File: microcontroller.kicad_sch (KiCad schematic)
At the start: 13 parts, among them SW3 System Reset, SW4 Boot Switch, U1 STM32F446RETx

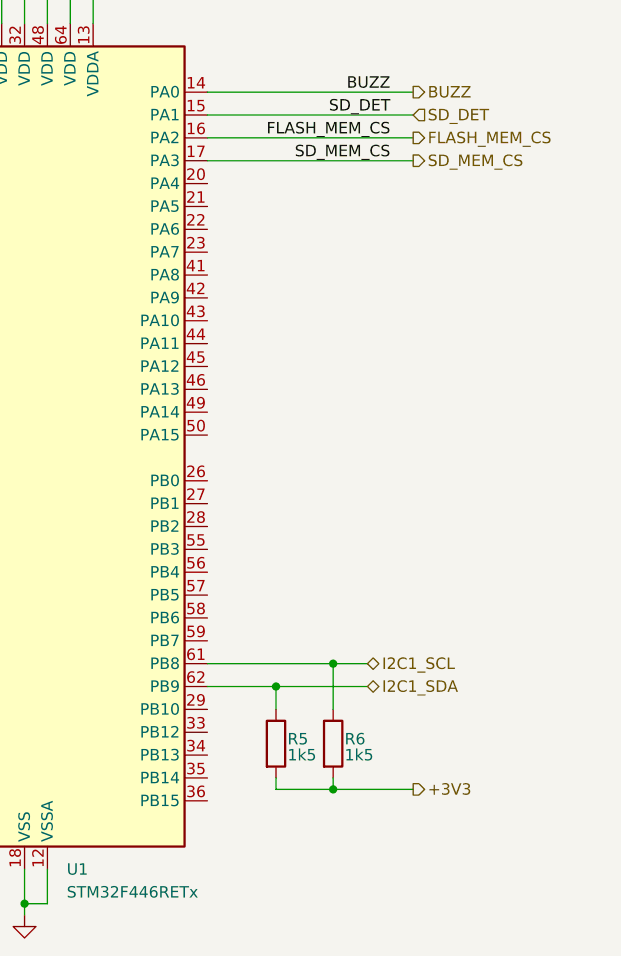
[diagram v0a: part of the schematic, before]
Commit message: more boilerplate for stm. and also power supply using LDO and USB
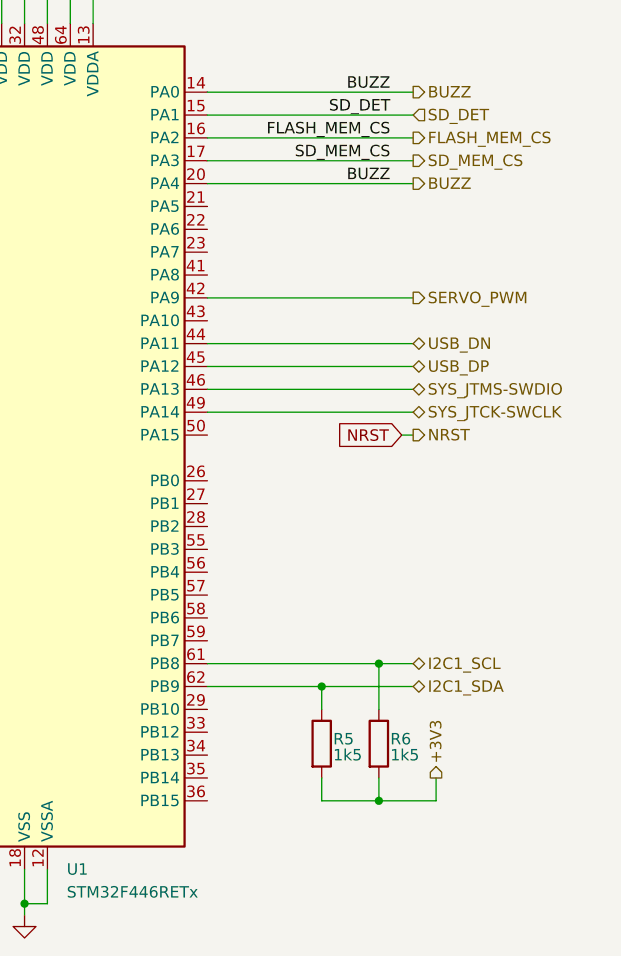
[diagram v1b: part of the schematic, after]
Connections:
- net BUZZ: now also U1.20 (PA4)
- net SERVO_PWM: now reaches U1.42 (PA9)
- net USB_DN: now reaches U1.44 (PA11)
- net USB_DP: now reaches U1.45 (PA12)
- net SYS_JTMS-SWDIO: now reaches U1.46 (PA13)
- net SYS_JTCK-SWCLK: now reaches U1.49 (PA14)
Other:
- moved on the sheet: R5, R6

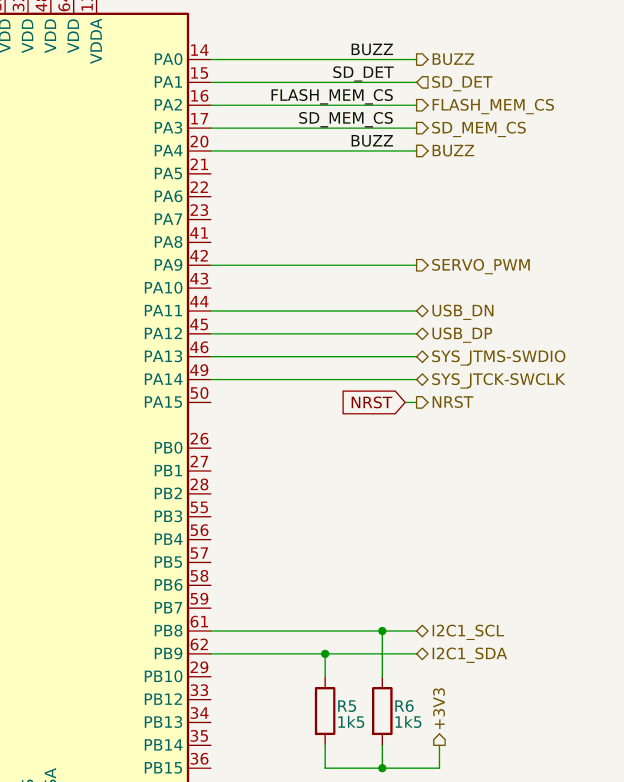
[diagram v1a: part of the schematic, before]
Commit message: base mcu decoupling cap routing
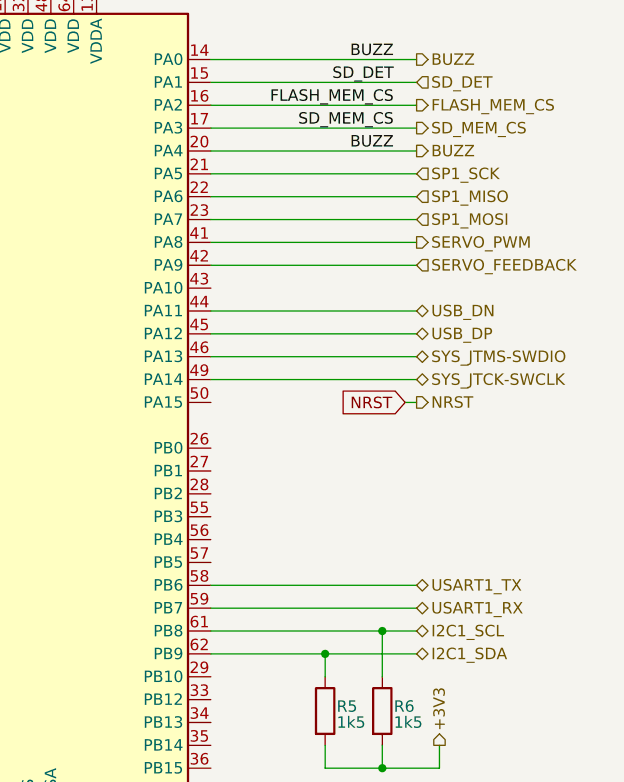
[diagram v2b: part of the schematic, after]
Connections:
- net SERVO_PWM: now also U1.41 (PA8); no longer U1.42 (PA9)
- net SP1_SCK: now reaches U1.21 (PA5)
- net SP1_MISO: now reaches U1.22 (PA6)
- net SP1_MOSI: now reaches U1.23 (PA7)
- net USART1_TX: now reaches U1.58 (PB6)
- net USART1_RX: now reaches U1.59 (PB7)
- new net SERVO_FEEDBACK: U1.42 (PA9)
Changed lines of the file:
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@@
+	(wire
+		(pts
+			(xy 146.05 133.35) (xy 168.91 133.35)
+		)
+		(stroke
+			(width 0)
+			(type default)
+		)
+	)
 	(wire
 		(pts
@@
 	(wire
 		(pts
+			(xy 146.05 130.81) (xy 168.91 130.81)
+		)
+		(stroke
+			(width 0)
+			(type default)
+		)
+	)
+	(wire
+		(pts
 			(xy 54.61 38.1) (xy 54.61 35.56)
 		)
@@
 	(wire
 		(pts
+			(xy 146.05 95.25) (xy 168.91 95.25)
+		)
+		(stroke
+			(width 0)
+			(type default)
+		)
+	)
+	(wire
+		(pts
 			(xy 158.75 138.43) (xy 168.91 138.43)
 		)
@@
 	(wire
 		(pts
+			(xy 146.05 85.09) (xy 168.91 85.09)
+		)
+		(stroke
+			(width 0)
+			(type default)
+		)
+	)
+	(wire
+		(pts
 			(xy 68.58 72.39) (xy 76.2 72.39)
 		)
@@
 	(wire
 		(pts
+			(xy 146.05 87.63) (xy 168.91 87.63)
+		)
+		(stroke
+			(width 0)
+			(type default)
+		)
+	)
+	(wire
+		(pts
 			(xy 130.81 60.96) (xy 133.35 60.96)
 		)
@@
 	(wire
 		(pts
-			(xy 146.05 95.25) (xy 168.91 95.25)
-		)
-		(stroke
-			(width 0)
-			(type default)
-		)
-	)
-	(wire
-		(pts
 			(xy 57.15 74.93) (xy 58.42 74.93)
 		)
@@
 	(wire
 		(pts
+			(xy 146.05 92.71) (xy 168.91 92.71)
+		)
+		(stroke
+			(width 0)
+			(type default)
+		)
+	)
+	(wire
+		(pts
 			(xy 146.05 138.43) (xy 158.75 138.43)
 		)
@@
 		(pts
 			(xy 165.1 135.89) (xy 165.1 140.97)
+		)
+		(stroke
+			(width 0)
+			(type default)
+		)
+	)
+	(wire
+		(pts
+			(xy 146.05 90.17) (xy 168.91 90.17)
 		)
 		(stroke
@@
 		)
 	)
+	(hierarchical_label "USART1_TX"
+		(shape bidirectional)
+		(at 168.91 130.81 0)
+		(effects
+			(font
+				(size 1.27 1.27)
+			)
+			(justify left)
+		)
+	)
 	(hierarchical_label "SD_DET"
 		(shape input)
@@
 	(hierarchical_label "SERVO_PWM"
 		(shape output)
-		(at 168.91 95.25 0)
+		(at 168.91 92.71 0)
 		(effects
 			(font
@@
 		)
 	)
+	(hierarchical_label "SERVO_FEEDBACK"
+		(shape input)
+		(at 168.91 95.25 0)
+		(effects
+			(font
+				(size 1.27 1.27)
+			)
+			(justify left)
+		)
+	)
 	(hierarchical_label "NRST"
 		(shape output)
 		(at 168.91 110.49 0)
+		(effects
+			(font
+				(size 1.27 1.27)
+			)
+			(justify left)
+		)
+	)
+	(hierarchical_label "SP1_MOSI"
+		(shape input)
+		(at 168.91 90.17 0)
+		(effects
+			(font
+				(size 1.27 1.27)
+			)
+			(justify left)
+		)
+	)
+	(hierarchical_label "USART1_RX"
+		(shape bidirectional)
+		(at 168.91 133.35 0)
 		(effects
 			(font
@@
 		)
 	)
+	(hierarchical_label "SP1_MISO"
+		(shape input)
+		(at 168.91 87.63 0)
+		(effects
+			(font
+				(size 1.27 1.27)
+			)
+			(justify left)
+		)
+	)
 	(hierarchical_label "I2C1_SCL"
 		(shape bidirectional)
@@
 		(effects
 			(font
+				(size 1.27 1.27)
+			)
+			(justify left)
+		)
+	)
+	(hierarchical_label "SP1_SCK"
+		(shape input)
+		(at 168.91 85.09 0)
+		(effects
+			(font
